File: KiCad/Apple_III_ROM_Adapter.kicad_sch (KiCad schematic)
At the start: 4 parts, among them U1 2532, U2 2764

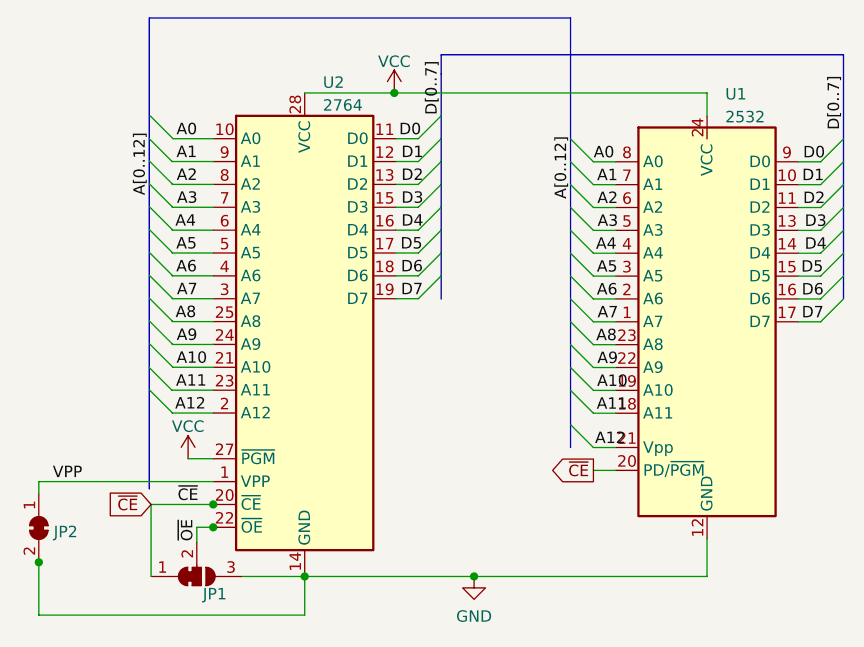
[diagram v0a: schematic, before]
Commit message: New PCB design, v2.0 EPROM rotated by 90 degrees, moved all the way back to align with the memory sandwich board.
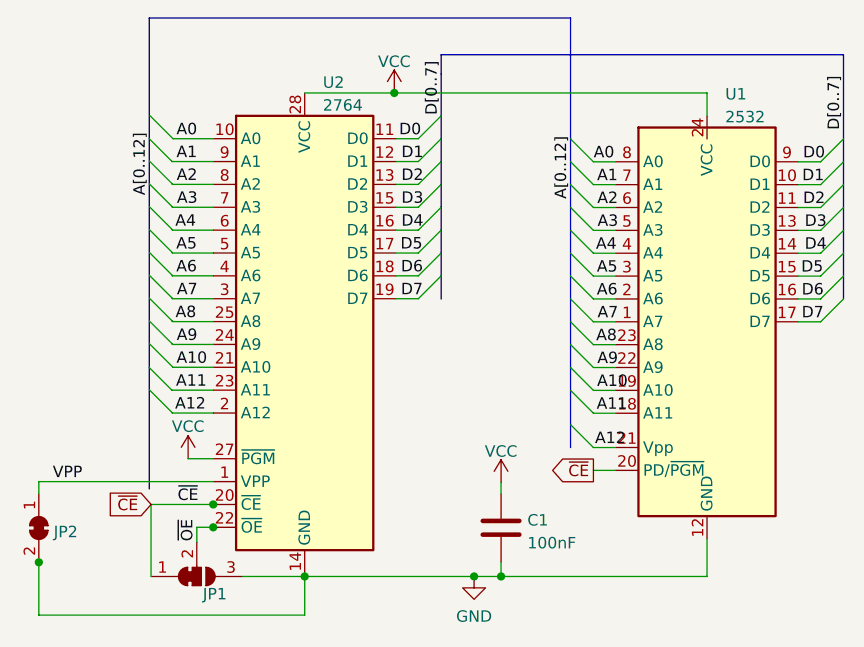
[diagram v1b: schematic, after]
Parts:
- added C1: 100nF, Capacitor_THT:C_Disc_D4.3mm_W1.9mm_P5.00mm, symbol Device:C
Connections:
- net GND: now also C1.2
- net VCC: now also C1.1
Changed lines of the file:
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@@
   (junction (at 100.076 100.6348) (diameter 0) (color 0 0 0 0)
   )
+  (junction (at 121.8946 100.6348) (diameter 0) (color 0 0 0 0)
+  )
   (junction (at 89.916 95.1738) (diameter 0) (color 0 0 0 0)
   )
@@
     (stroke (width 0) (type default) (color 0 0 0 0))
   )
+  (wire (pts (xy 121.8946 99.0346) (xy 121.8946 100.6348))
+    (stroke (width 0) (type default) (color 0 0 0 0))
+  )
   (bus (pts (xy 115.2398 49.4538) (xy 115.2398 44.8056))
     (stroke (width 0) (type default) (color 0 0 0 0))
@@
     (stroke (width 0) (type default) (color 0 0 0 0))
   )
+  (wire (pts (xy 121.8946 100.6348) (xy 144.78 100.6348))
+    (stroke (width 0) (type default) (color 0 0 0 0))
+  )
   (wire (pts (xy 134.62 82.4992) (xy 132.1562 82.4992))
     (stroke (width 0) (type default) (color 0 0 0 0))
@@
     (stroke (width 0) (type default) (color 0 0 0 0))
   )
+  (wire (pts (xy 121.8946 90.2208) (xy 121.8946 91.4146))
+    (stroke (width 0) (type default) (color 0 0 0 0))
+  )
   (bus (pts (xy 129.6162 38.5826) (xy 129.6162 42.037))
     (stroke (width 0) (type default) (color 0 0 0 0))
@@
     (stroke (width 0) (type default) (color 0 0 0 0))
   )
-  (wire (pts (xy 118.8974 100.6348) (xy 144.78 100.6348))
+  (wire (pts (xy 118.8974 100.6348) (xy 121.8946 100.6348))
     (stroke (width 0) (type default) (color 0 0 0 0))
   )
@@
     (pin "8")
     (pin "9")
+  )
+  (symbol (lib_id "power:VCC") (at 121.8946 90.2208 0) (unit 1)
+    (in_bom yes) (on_board yes)
+    (property "Reference" "#PWR0104" (id 0) (at 121.8946 94.0308 0)
+      (effects (font (size 1.27 1.27)) hide)
+    )
+    (property "Value" "VCC" (id 1) (at 121.8946 86.741 0))
+    (property "Footprint" "" (id 2) (at 121.8946 90.2208 0)
+      (effects (font (size 1.27 1.27)) hide)
+    )
+    (property "Datasheet" "" (id 3) (at 121.8946 90.2208 0)
+      (effects (font (size 1.27 1.27)) hide)
+    )
+    (pin "1")
+  )
+  (symbol (lib_id "Device:C") (at 121.8946 95.2246 0) (unit 1)
+    (in_bom yes) (on_board yes) (fields_autoplaced)
+    (property "Reference" "C1" (id 0) (at 124.8156 94.3899 0)
+      (effects (font (size 1.27 1.27)) (justify left))
+    )
+    (property "Value" "100nF" (id 1) (at 124.8156 96.9268 0)
+      (effects (font (size 1.27 1.27)) (justify left))
+    )
+    (property "Footprint" "Capacitor_THT:C_Disc_D4.3mm_W1.9mm_P5.00mm" (id 2) (at 122.8598 99.0346 0)
+      (effects (font (size 1.27 1.27)) hide)
+    )
+    (property "Datasheet" "~" (id 3) (at 121.8946 95.2246 0)
+      (effects (font (size 1.27 1.27)) hide)
+    )
+    (pin "1")
+    (pin "2")
   )
   (symbol (lib_id "Memory_EPROM:2764") (at 100.076 72.3138 0) (unit 1)
@@
       (reference "#PWR0103") (unit 1) (value "VCC") (footprint "")
     )
+    (path "/aa70deea-44d6-4557-bbe5-4d257568a55d"
+      (reference "#PWR0104") (unit 1) (value "VCC") (footprint "")
+    )
+    (path "/f2bb7b12-af32-48b8-8d13-b306a0496764"
+      (reference "C1") (unit 1) (value "100nF") (footprint "Capacitor_THT:C_Disc_D4.3mm_W1.9mm_P5.00mm")
+    )
     (path "/5162054a-9a9f-46e2-a196-7f5809e2a840"
